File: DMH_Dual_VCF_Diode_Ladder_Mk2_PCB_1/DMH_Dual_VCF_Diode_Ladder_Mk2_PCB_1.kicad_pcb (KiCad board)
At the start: 2 copper layers, 146 x 175 mm, 226 parts, among them J0 Conn_01x01, J1 TS_Jack_6.35mm_Sw, J10 TS_Jack_6.35mm_Sw, J100 IDC_02x08, J11 TS_Jack_6.35mm_Sw, J12 TS_Jack_6.35mm_Sw, J13 TS_Jack_6.35mm_Sw, J14 TS_Jack_6.35mm_Sw, J15 Conn_01x08_PinHeader, J16 Conn_01x08_PinHeader, J17 Conn_01x06_PinHeader, J18 Conn_01x06_PinHeader, J19 Conn_01x04_PinHeader, J2 TS_Jack_6.35mm_Sw, J20 Conn_01x04_PinHeader, J200 IDC_02x05, J21 Conn_01x06_PinHeader, J210 IDC_02x05, J22 Conn_01x06_PinHeader, J23 Conn_01x04_PinHeader, J3 TS_Jack_6.35mm_Sw, J4 TS_Jack_6.35mm_Sw, J5 TS_Jack_6.35mm_Sw, J6 TS_Jack_6.35mm_Sw, J7 TS_Jack_6.35mm_Sw, J8 TS_Jack_6.35mm_Sw, J9 TS_Jack_6.35mm_Sw, Q1 BC548, Q2 BC548, Q3 BC548, Q4 BC548, Q5 BC548, Q6 BC548, Q7 BC548, Q8 BC548, U1 TL074, U10 TL074, U2 TL074, U3 TL074, U4 TL074, U5 TL074, U6 TL074, U7 TL074, U8 TL074, U9 TL074

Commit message: Changed VCA CV summing stage feedback to 100k
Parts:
- R112, R129, R77, R83: value 82k -> 100k

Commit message: Adding buffered input to CV3 - in progress
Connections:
- J15 pad 2: /CV Processing/CV3 A Input -> Net-(J15B-Pin_2)
- J16 pad 2: /CV Processing/CV3 B Input -> Net-(J16B-Pin_2)
- U7 pad 5: GND -> /CV Processing/CV3 A Input
- U7 pad 6: Net-(U7B--) -> Net-(J15B-Pin_2)
- U7 pad 7: Net-(U7B--) -> Net-(J15B-Pin_2)
- U8 pad 10: GND -> /CV Processing/CV3 B Input
- U8 pad 8: Net-(U8C--) -> Net-(J16B-Pin_2)
- U8 pad 9: Net-(U8C--) -> Net-(J16B-Pin_2)
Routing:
- net Net-(J15B-Pin_2): track 0.00 -> 60.8 mm
- net /CV Processing/CV3 A Input: track 86.8 -> 57.7 mm
- net Net-(U8C--): track 2.54 -> 0.00 mm
- net Net-(U7B--): track 2.54 -> 0.00 mm
- net Net-(J16B-Pin_2): track 0.00 -> 2.54 mm
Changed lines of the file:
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@@
 	(net 132 "/Resonance A CV/Res CV")
 	(net 133 "Net-(R88-Pad1)")
-	(net 134 "Net-(U7B--)")
+	(net 134 "Net-(J15B-Pin_2)")
 	(net 135 "Net-(Q5-B)")
 	(net 136 "Net-(R94-Pad1)")
@@
 	(net 167 "Net-(R124-Pad1)")
 	(net 168 "Net-(U6C--)")
-	(net 169 "Net-(U8C--)")
+	(net 169 "Net-(J16B-Pin_2)")
 	(net 170 "Net-(U9A--)")
 	(net 171 "Net-(U10D--)")
@@
 			(layers "*.Cu" "*.Mask")
 			(remove_unused_layers no)
-			(net 32 "/CV Processing/CV3 A Input")
+			(net 134 "Net-(J15B-Pin_2)")
 			(pinfunction "Pin_2")
 			(pintype "passive")
@@
 			(layers "*.Cu" "*.Mask")
 			(remove_unused_layers no)
-			(net 47 "/CV Processing/CV3 B Input")
+			(net 169 "Net-(J16B-Pin_2)")
 			(pinfunction "Pin_2")
 			(pintype "passive")
@@
 			(layers "*.Cu" "*.Mask")
 			(remove_unused_layers no)
-			(net 169 "Net-(U8C--)")
+			(net 169 "Net-(J16B-Pin_2)")
 			(pintype "output")
 		)
@@
 			(layers "*.Cu" "*.Mask")
 			(remove_unused_layers no)
-			(net 169 "Net-(U8C--)")
+			(net 169 "Net-(J16B-Pin_2)")
 			(pinfunction "-")
 			(pintype "input")
@@
 			(layers "*.Cu" "*.Mask")
 			(remove_unused_layers no)
-			(net 1 "GND")
+			(net 47 "/CV Processing/CV3 B Input")
 			(pinfunction "+")
 			(pintype "input")
@@
 			(layers "*.Cu" "*.Mask")
 			(remove_unused_layers no)
-			(net 1 "GND")
+			(net 32 "/CV Processing/CV3 A Input")
 			(pinfunction "+")
 			(pintype "input")
@@
 			(layers "*.Cu" "*.Mask")
 			(remove_unused_layers no)
-			(net 134 "Net-(U7B--)")
+			(net 134 "Net-(J15B-Pin_2)")
 			(pinfunction "-")
 			(pintype "input")
@@
 			(layers "*.Cu" "*.Mask")
 			(remove_unused_layers no)
-			(net 134 "Net-(U7B--)")
+			(net 134 "Net-(J15B-Pin_2)")
 			(pintype "output")
 		)
@@
 	)
 	(segment
-		(start 72.5 192)
-		(end 80 192)
+		(start 80 192)
+		(end 80.9025 191.0975)
 		(width 0.2)
 		(layer "F.Cu")
@@
 	)
 	(segment
-		(start 64.25 183.75)
-		(end 72.5 192)
+		(start 83.31 191.0975)
+		(end 84.46 192.2475)
 		(width 0.2)
 		(layer "F.Cu")
@@
 	)
 	(segment
-		(start 83.31 191.0975)
-		(end 84.46 192.2475)
+		(start 80.9025 191.0975)
+		(end 83.31 191.0975)
 		(width 0.2)
 		(layer "F.Cu")
@@
 	)
 	(segment
-		(start 80.9025 191.0975)
-		(end 83.31 191.0975)
+		(start 63 183.75)
+		(end 71.25 192)
 		(width 0.2)
 		(layer "F.Cu")
@@
 	)
 	(segment
-		(start 80 192)
-		(end 80.9025 191.0975)
+		(start 71.25 192)
+		(end 80 192)
 		(width 0.2)
 		(layer "F.Cu")
@@
 	(segment
 		(start 52.5 183.75)
-		(end 64.25 183.75)
+		(end 63 183.75)
 		(width 0.2)
 		(layer "F.Cu")
@@
 	)
 	(segment
-		(start 73 189.75)
-		(end 70.815686 189.75)
+		(start 69.5671 189.75)
+		(end 59.0681 179.251)
 		(width 0.2)
 		(layer "F.Cu")
@@
 	)
 	(segment
-		(start 31.14 144.39)
-		(end 29.39 144.39)
+		(start 44.75 171.5)
+		(end 44.75 170.25)
 		(width 0.2)
 		(layer "F.Cu")
@@
 	)
 	(segment
-		(start 32.75 146)
-		(end 31.14 144.39)
+		(start 50.5 167.75)
+		(end 51.25 167)
 		(width 0.2)
 		(layer "F.Cu")
@@
 	)
 	(segment
-		(start 60.315686 179.25)
-		(end 49.25 179.25)
+		(start 51.25 167)
+		(end 51.25 157.835)
 		(width 0.2)
 		(layer "F.Cu")
@@
 	)
 	(segment
-		(start 28.75 143.75)
-		(end 28.75 131.79)
+		(start 73 189.75)
+		(end 69.5671 189.75)
 		(width 0.2)
 		(layer "F.Cu")
@@
 	)
 	(segment
-		(start 28.75 131.79)
-		(end 30 130.54)
+		(start 59.0681 179.251)
+		(end 52.501 179.251)
 		(width 0.2)
 		(layer "F.Cu")
@@
 	)
 	(segment
-		(start 32.75 162.75)
-		(end 32.75 146)
+		(start 44.75 170.25)
+		(end 47.25 167.75)
 		(width 0.2)
 		(layer "F.Cu")
@@
 	)
 	(segment
-		(start 49.25 179.25)
-		(end 32.75 162.75)
+		(start 52.501 179.251)
+		(end 44.75 171.5)
 		(width 0.2)
 		(layer "F.Cu")
@@
 	)
 	(segment
-		(start 70.815686 189.75)
-		(end 60.315686 179.25)
+		(start 47.25 167.75)
+		(end 50.5 167.75)
 		(width 0.2)
 		(layer "F.Cu")
@@
 	)
 	(segment
-		(start 29.39 144.39)
-		(end 28.75 143.75)
+		(start 51.25 157.835)
+		(end 53.8 155.285)
 		(width 0.2)
 		(layer "F.Cu")
@@
 	)
 	(segment
+		(start 73.437995 187.942)
+		(end 73.436995 187.941)
+		(width 0.2)
+		(layer "F.Cu")
+		(net 64)
+	)
+	(segment
+		(start 54.29 178.85)
+		(end 46.19 170.75)
+		(width 0.2)
+		(layer "F.Cu")
+		(net 64)
+	)
+	(segment
+		(start 73.436995 187.941)
+		(end 72.563005 187.941)
+		(width 0.2)
+		(layer "F.Cu")
+		(net 64)
+	)
+	(segment
+		(start 72.562005 187.942)
+		(end 68.3262 187.942)
+		(width 0.2)
+		(layer "F.Cu")
+		(net 64)
+	)
+	(segment
+		(start 59.2342 178.85)
+		(end 59.1 178.85)
+		(width 0.2)
+		(layer "F.Cu")
+		(net 64)
+	)
+	(segment
+		(start 68.3262 187.942)
+		(end 59.4691 179.0849)
+		(width 0.2)
+		(layer "F.Cu")
+		(net 64)
+	)
+	(segment
 		(start 112.9975 192.2475)
 		(end 108.692 187.942)
@@
 	)
 	(segment
-		(start 108.692 187.942)
-		(end 69.573372 187.942)
+		(start 59.1 178.85)
+		(end 58.902 178.85)
 		(width 0.2)
 		(layer "F.Cu")
@@
 	)
 	(segment
-		(start 69.573372 187.942)
-		(end 60.481372 178.85)
+		(start 72.563005 187.941)
+		(end 72.562005 187.942)
 		(width 0.2)
 		(layer "F.Cu")
@@
 	)
 	(segment
+		(start 58.902 178.85)
+		(end 54.29 178.85)
+		(width 0.2)
+		(layer "F.Cu")
+		(net 64)
+	)
+	(segment
 		(start 115.2875 190)
 		(end 135.25 190)
@@
 	)
 	(segment
-		(start 54.29 178.85)
-		(end 46.19 170.75)
+		(start 59.4691 179.0849)
+		(end 59.2342 178.85)
 		(width 0.2)
 		(layer "F.Cu")
@@
 	)
 	(segment
-		(start 60.481372 178.85)
-		(end 54.29 178.85)
+		(start 108.692 187.942)
+		(end 73.437995 187.942)
 		(width 0.2)
 		(layer "F.Cu")
@@
 	)
 	(segment
+		(start 38.551 152.801)
+		(end 38.551 144.148)
+		(width 0.2)
+		(layer "B.Cu")
+		(net 134)
+	)
+	(segment
+		(start 53.8 157.825)
+		(end 49.975 154)
+		(width 0.2)
+		(layer "B.Cu")
+		(net 134)
+	)
+	(segment
+		(start 47.291 134.291)
+		(end 43.54 130.54)
+		(width 0.2)
+		(layer "B.Cu")
+		(net 134)
+	)
+	(segment
+		(start 38.551 144.148)
+		(end 47.291 135.408)
+		(width 0.2)
+		(layer "B.Cu")
+		(net 134)
+	)
+	(segment
+		(start 47.291 135.408)
+		(end 47.291 134.291)
+		(width 0.2)
+		(layer "B.Cu")
+		(net 134)
+	)
+	(segment
 		(start 53.8 160.365)
 		(end 53.8 157.825)
 		(width 0.2)
 		(layer "B.Cu")
+		(net 134)
+	)
+	(segment
+		(start 49.975 154)
+		(end 39.75 154)
+		(width 0.2)
+		(layer "B.Cu")
+		(net 134)
+	)
+	(segment
+		(start 43.54 130.54)
+		(end 30 130.54)
+		(width 0.2)
+		(layer "B.Cu")
+		(net 134)
+	)
+	(segment
+		(start 39.75 154)
+		(end 38.551 152.801)
+		(width 0.2)
+		(layer "B.Cu")

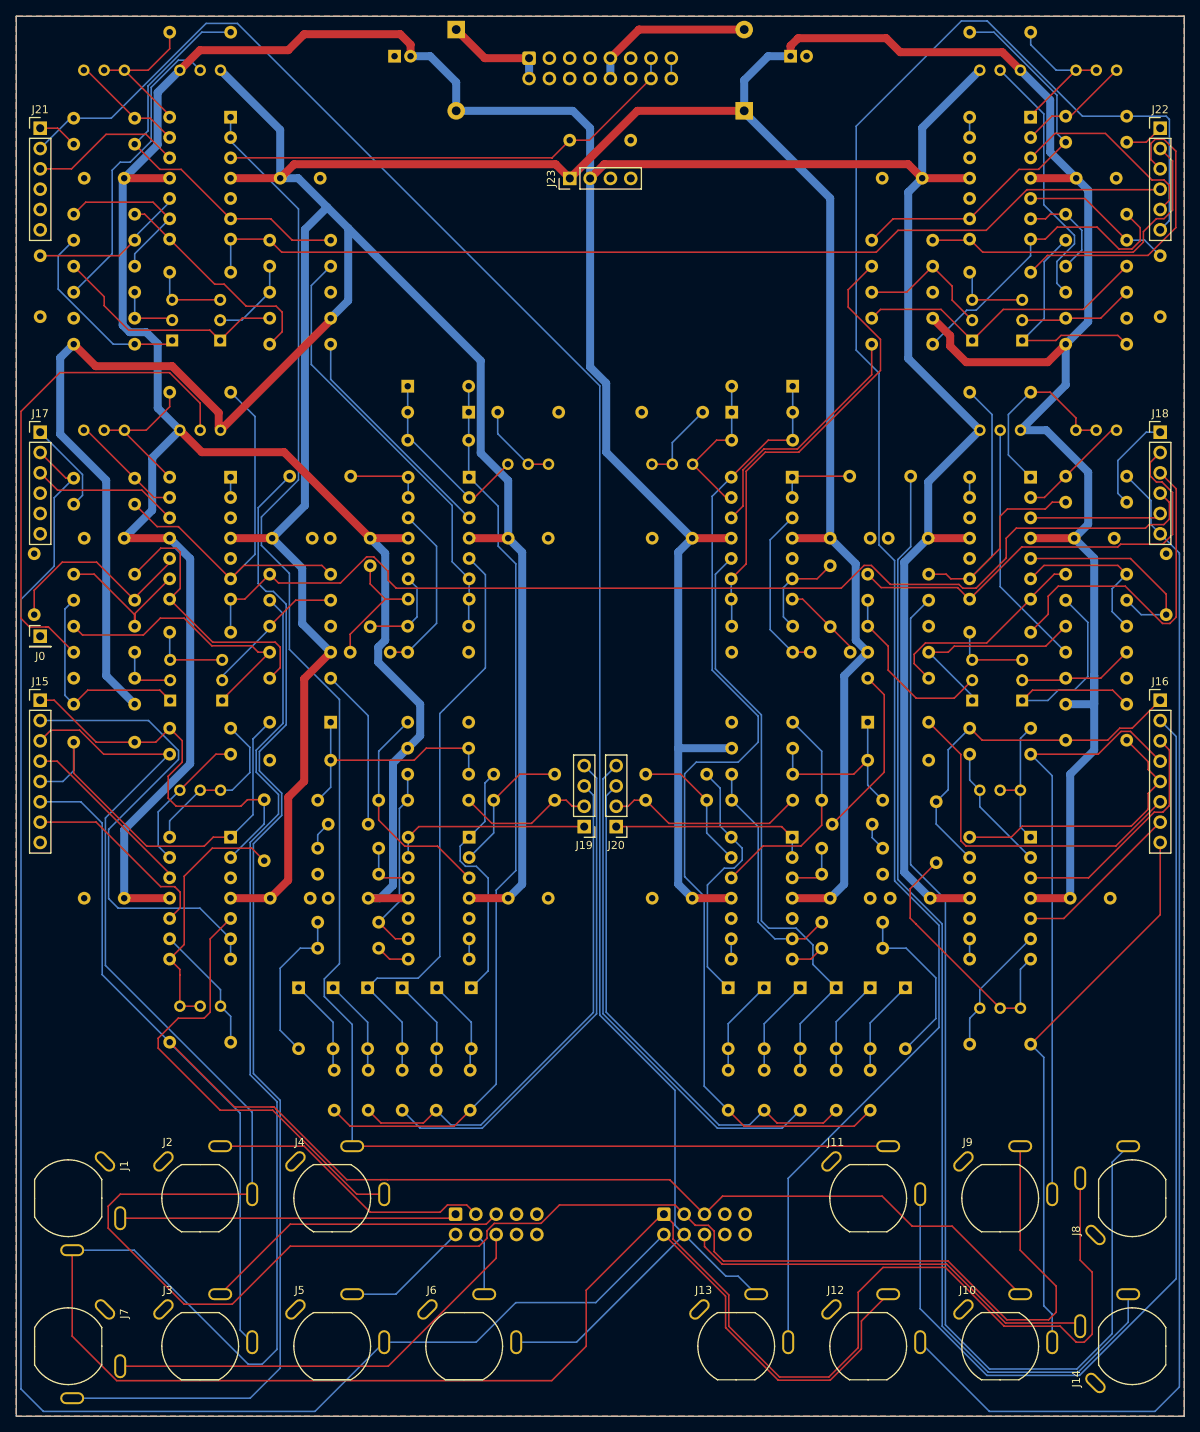
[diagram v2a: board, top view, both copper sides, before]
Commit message: Added buffering to each CV 3 input separately
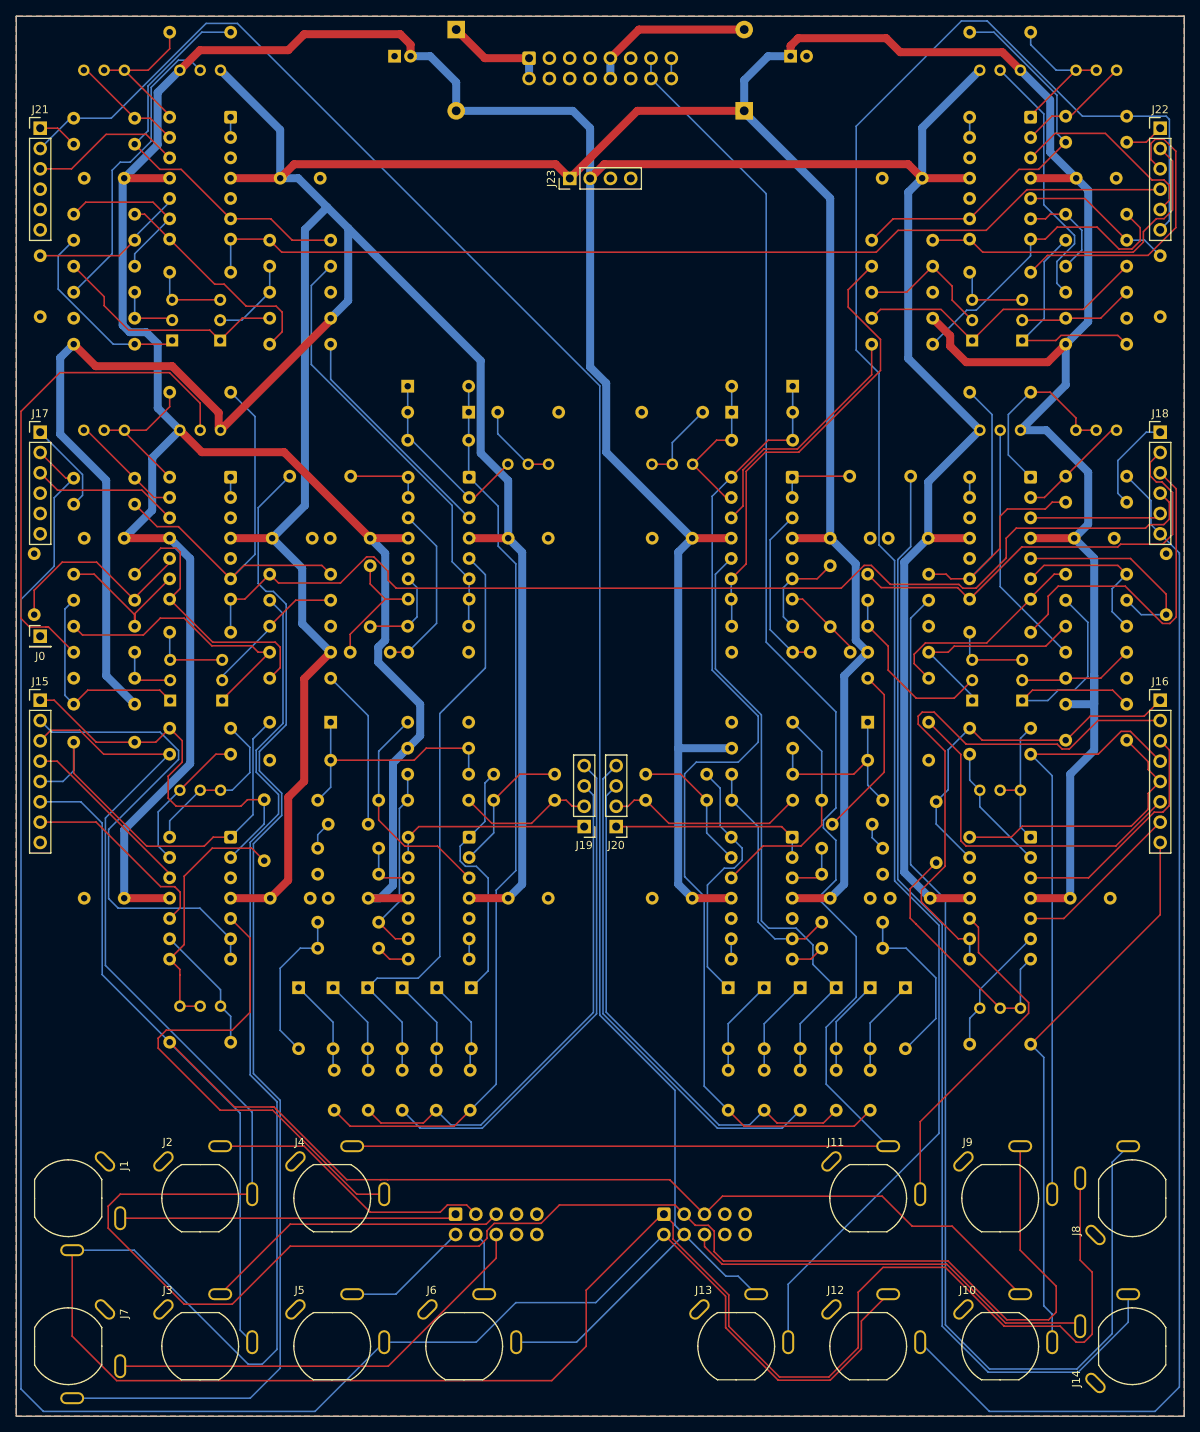
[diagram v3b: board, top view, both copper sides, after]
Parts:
- removed R96: 5M, Resistor_THT:R_Axial_DIN0207_L6.3mm_D2.5mm_P7.62mm_Horizontal
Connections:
- J100 pad 7a: Net-(J100-Pin_7a) -> /Inputs and Outputs A/CV 3 TN
- J100 pad 7b: Net-(J100-Pin_7a) -> /Inputs and Outputs A/CV 3 TN
- U1 pad 1: /Inputs and Outputs A/CV 3 TN -> Net-(U1A--)
- U1 pad 2: /Inputs and Outputs A/CV 3 TN -> Net-(U1A--)
- U1 pad 3: Net-(J100-Pin_7a) -> GND
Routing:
- net /CV Processing/CV3 B Input: track 125.4 -> 43.1 mm
- net Net-(J16B-Pin_2): track 2.54 -> 70.1 mm
- net Net-(J100-Pin_7a): track 59.2 -> 0.00 mm
- net /Inputs and Outputs A/CV 3 TN: track 207.3 -> 221.2 mm
- net /CV Processing/CV3 A Input: track 57.7 -> 62.6 mm
- net Net-(U1A--): track 0.00 -> 2.98 mm
